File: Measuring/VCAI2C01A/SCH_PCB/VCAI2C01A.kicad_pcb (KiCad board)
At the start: 2 copper layers, 60.5 x 40.1 mm, 74 parts, among them J10 JUMP2_2x1, J11 JUMP2_2x1, J13 JUMP_5X2, J14 JUMP_2x1, J15 JUMP_2x1, J16 JUMP_2x1, J17 JUMP_2x1, J18 JUMP_2x1, J19 JUMP_2x1, J2 CONN_2, J20 JUMP_2x1, J21 JUMP_2x1, J22 JUMP_2x1, J23 JUMP_2x1, J3 JUMP_2x1, J4 CONN_2, J5 JUMP_2x1, J6 CONN_2, J7 JUMP_2x1, J8 CONN_2, J9 JUMP_2x1, M1 HOLE, M2 HOLE, M3 HOLE, M4 HOLE, U1 TLC27L2ID, U2 TLC27L2ID, U3 MCP3424

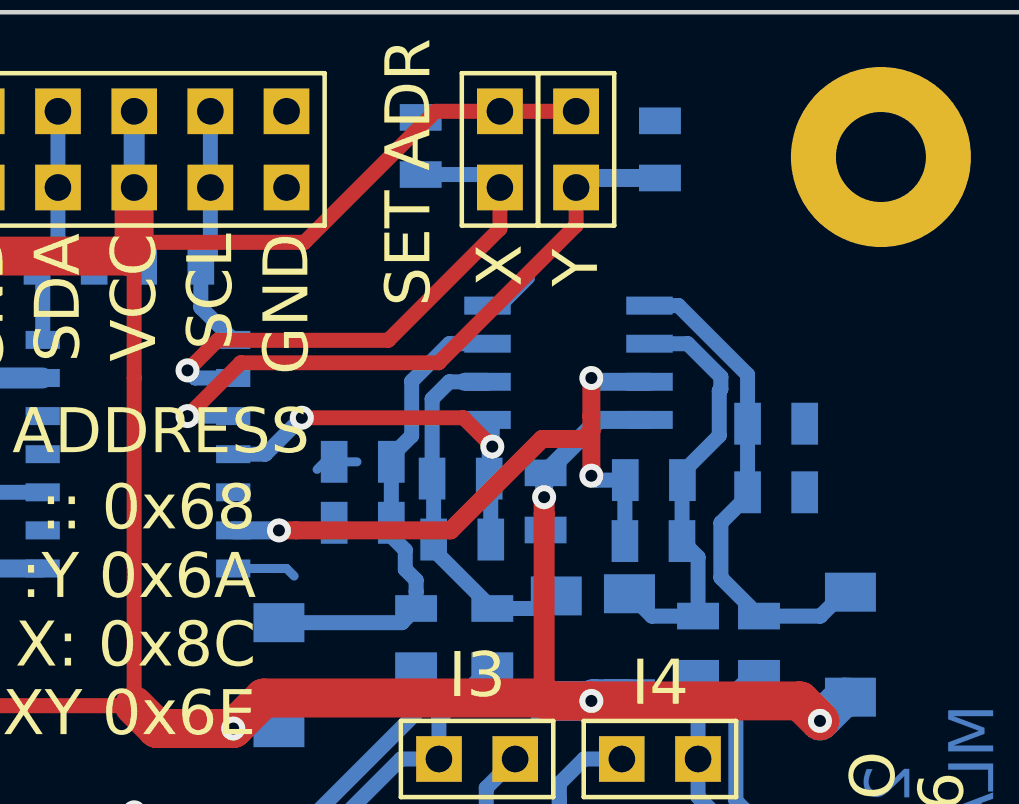
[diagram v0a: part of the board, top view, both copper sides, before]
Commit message: 
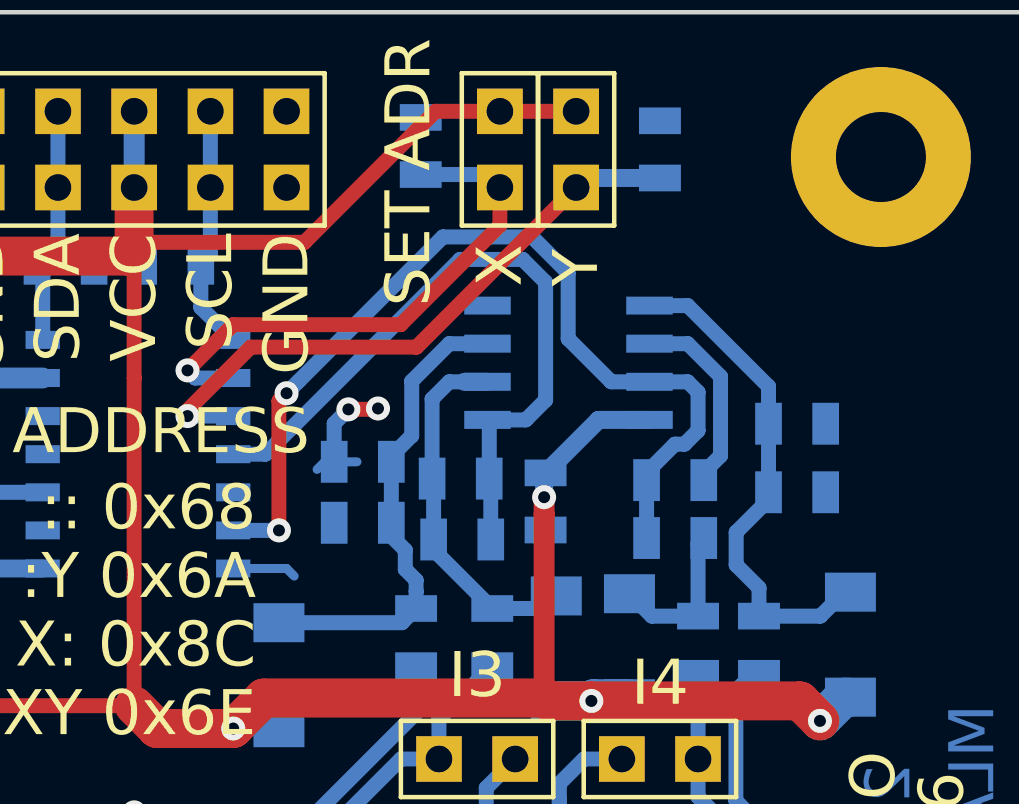
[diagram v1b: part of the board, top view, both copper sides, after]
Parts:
- moved R20 0.73 mm to (49.0, -22.9)
- moved C11 0.71 mm to (49.0, -24.8)
- moved C9 0.70 mm to (53.1, -24.4)
- moved R18 0.70 mm to (53.1, -26.7)
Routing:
- net /OUT3: track 14.0 -> 23.9 mm, vias 2 -> 0
- net /OUT4: track 21.8 -> 31.3 mm, vias 3 -> 2
- net /IN4_2-: track 14.3 -> 11.9 mm
- net GND: track 39.0 -> 40.7 mm, vias 18 -> 20
- net /A1: track 21.3 -> 20.7 mm

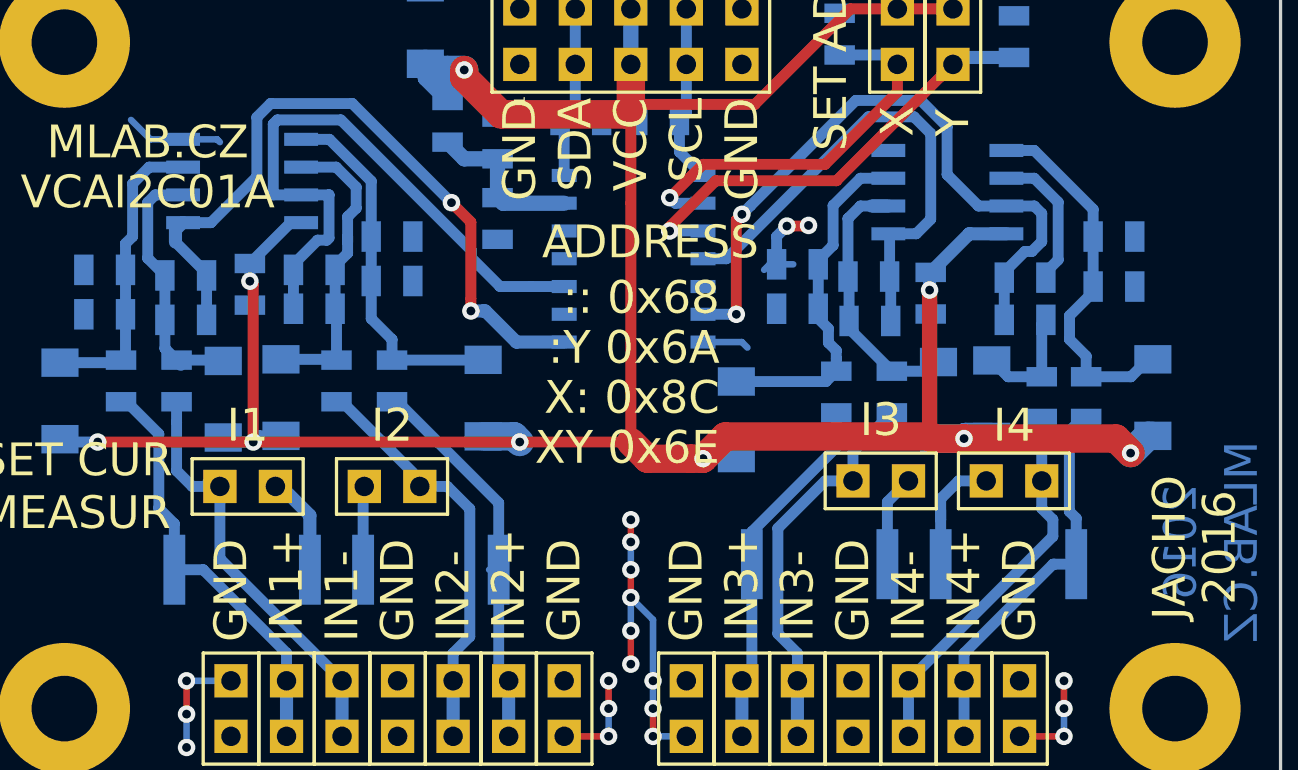
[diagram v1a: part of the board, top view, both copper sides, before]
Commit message: zlepseni layoutu.
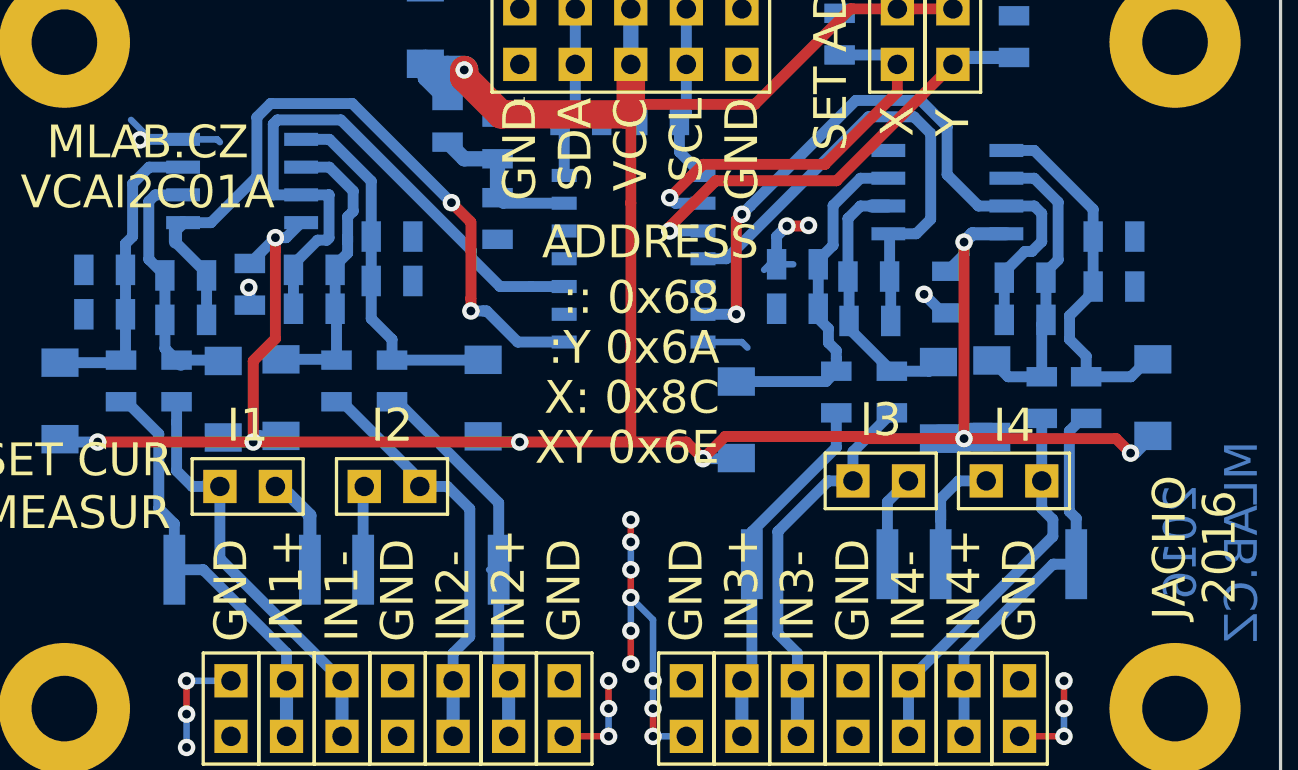
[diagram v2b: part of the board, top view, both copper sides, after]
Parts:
- moved C12 0.76 mm to (45.5, -24.1)
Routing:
- net GND: track 40.7 -> 44.9 mm, vias 20 -> 23
- net VCC: track 141.8 -> 144.9 mm
- net /IN4_2-: track 11.9 -> 13.8 mm

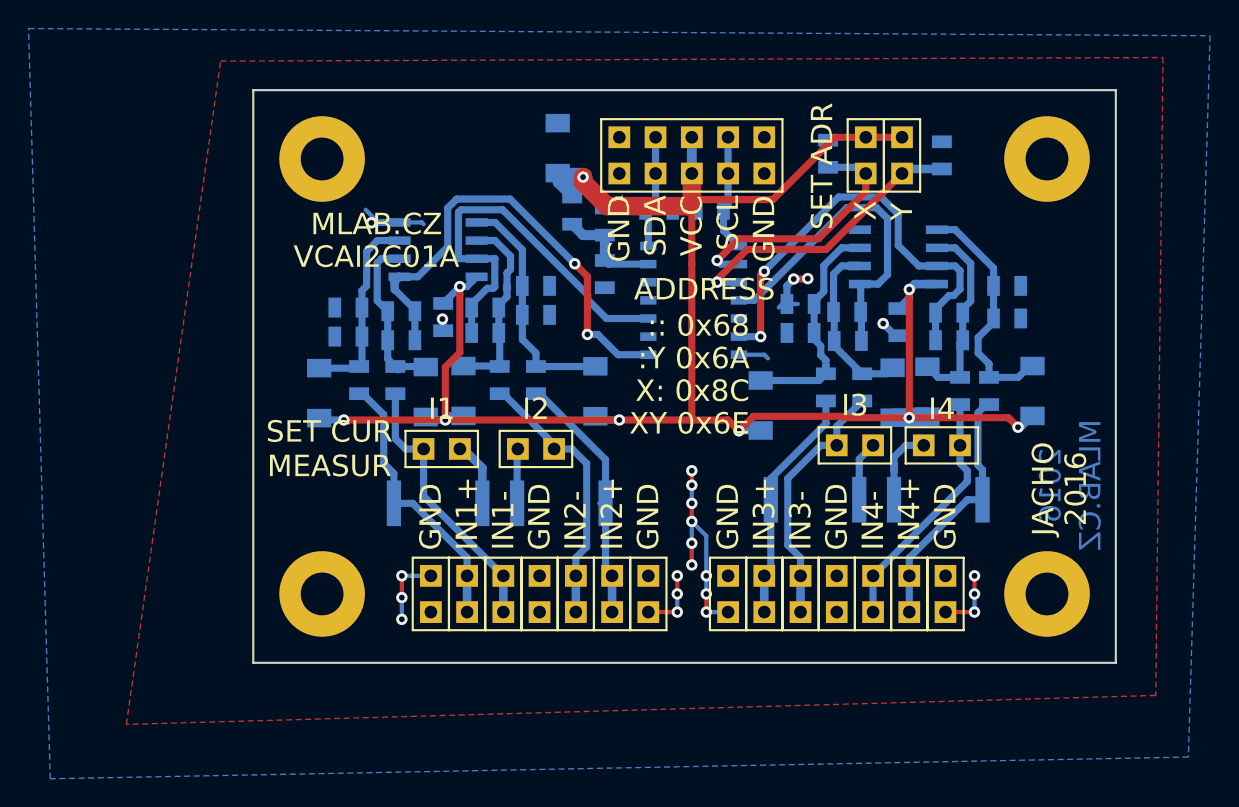
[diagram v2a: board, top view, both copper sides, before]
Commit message: 
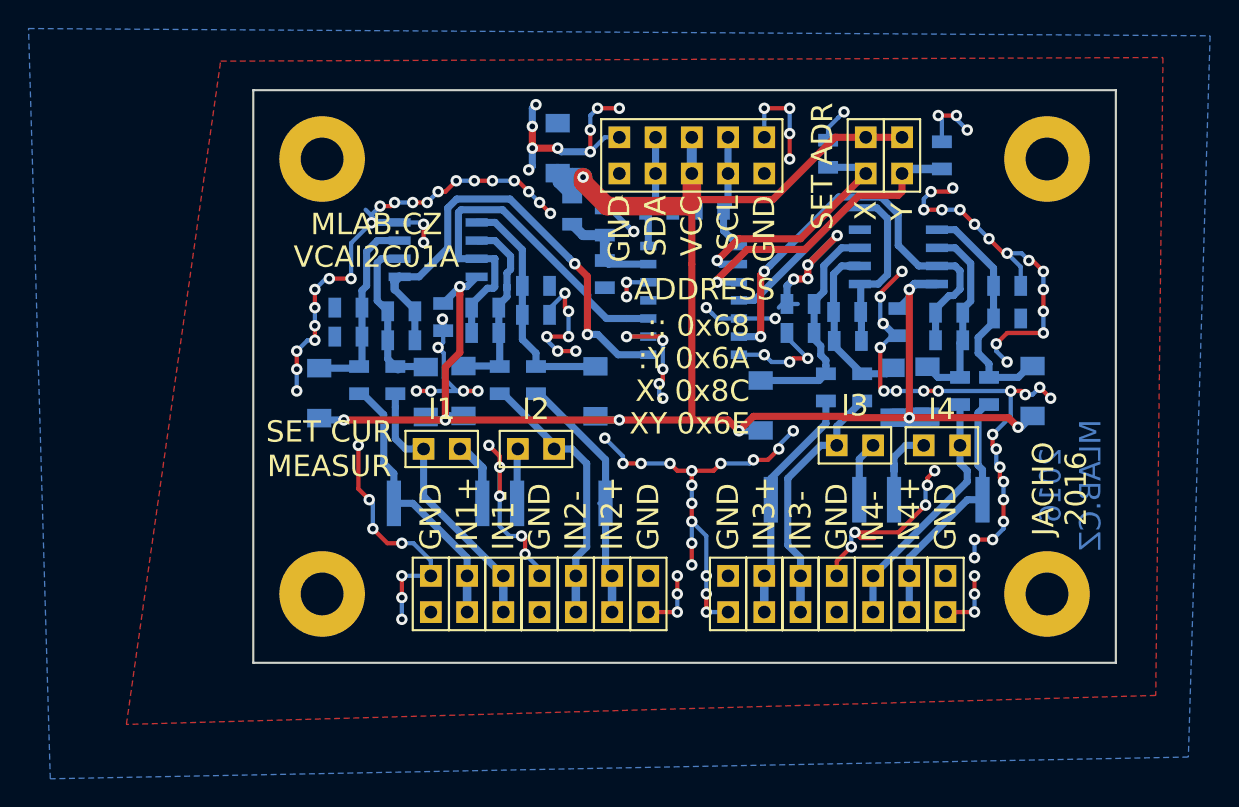
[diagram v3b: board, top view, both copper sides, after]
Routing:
- net GND: track 44.9 -> 277.0 mm, vias 23 -> 146
- net /A1: track 20.7 -> 21.4 mm
- net /A0: track 18.1 -> 17.4 mm

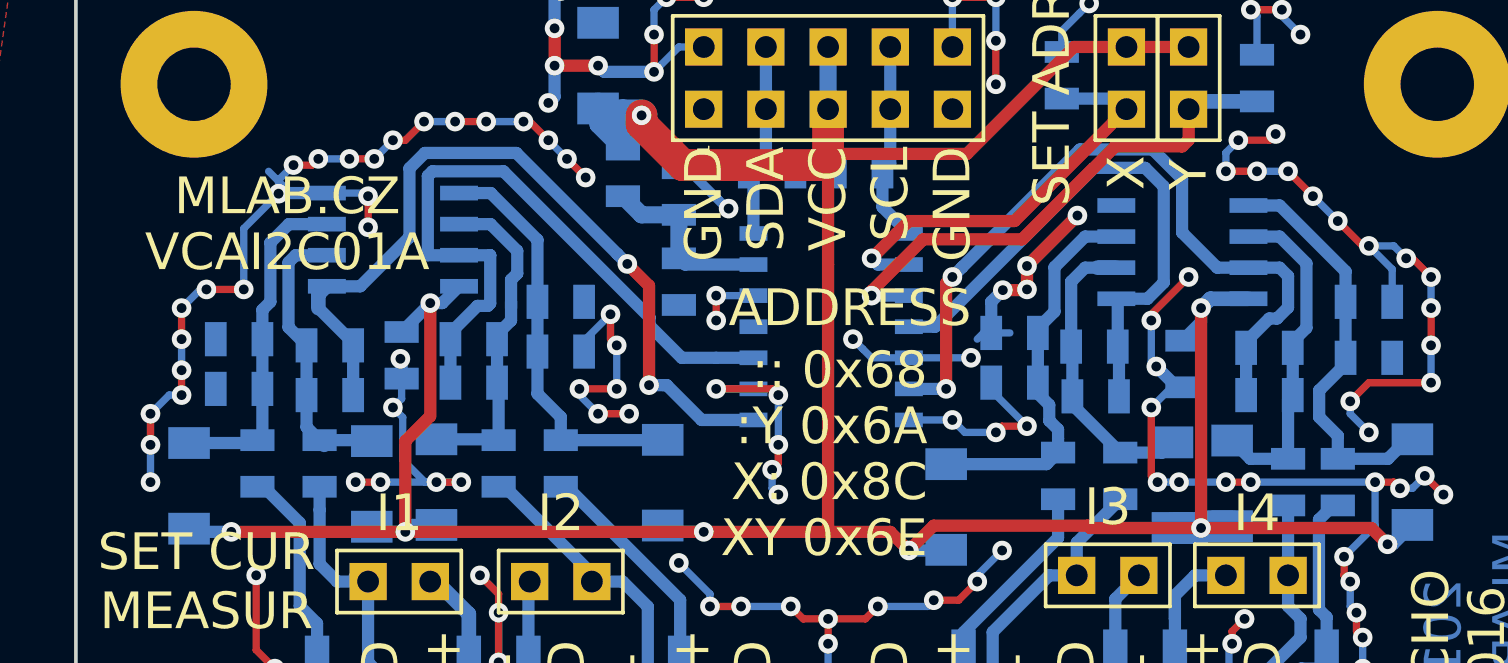
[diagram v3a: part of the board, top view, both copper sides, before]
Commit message: 
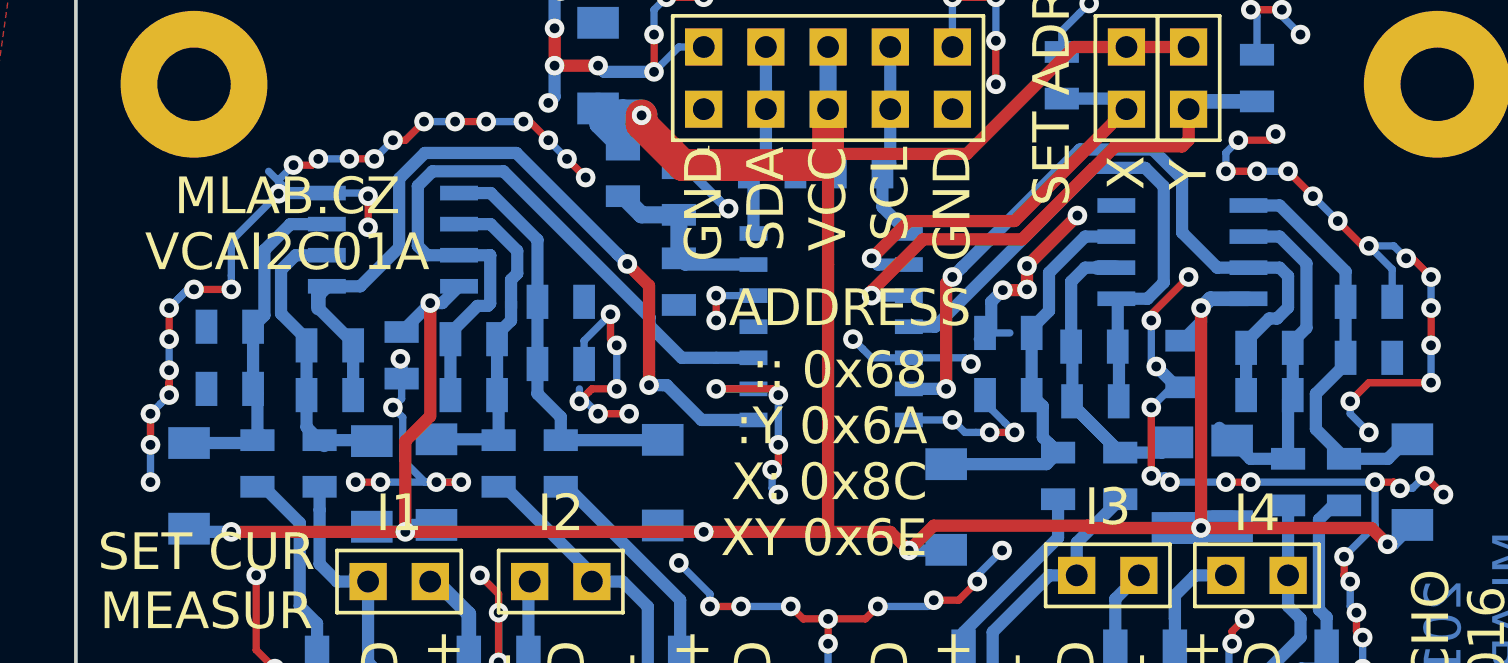
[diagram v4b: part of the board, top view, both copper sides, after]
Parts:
- moved C1 0.63 mm to (6.54, -25.7)
- moved C8 0.57 mm to (38.4, -22.9)
- moved R8 0.51 mm to (20.1, -24.1)
- moved C7 0.51 mm to (16.5, -22.9)
- moved R7 0.38 mm to (6.54, -23.1)
- moved R16 0.25 mm to (52.1, -19.3)
- moved R17 0.25 mm to (38.4, -25.4)
- moved C10 0.20 mm to (41.9, -22.6)
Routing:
- net /IN3_2-: track 13.2 -> 16.1 mm
- net GND: track 277.0 -> 278.8 mm
- net /IN3_2+: track 16.9 -> 17.7 mm
- net /IN4_2-: track 13.8 -> 14.5 mm

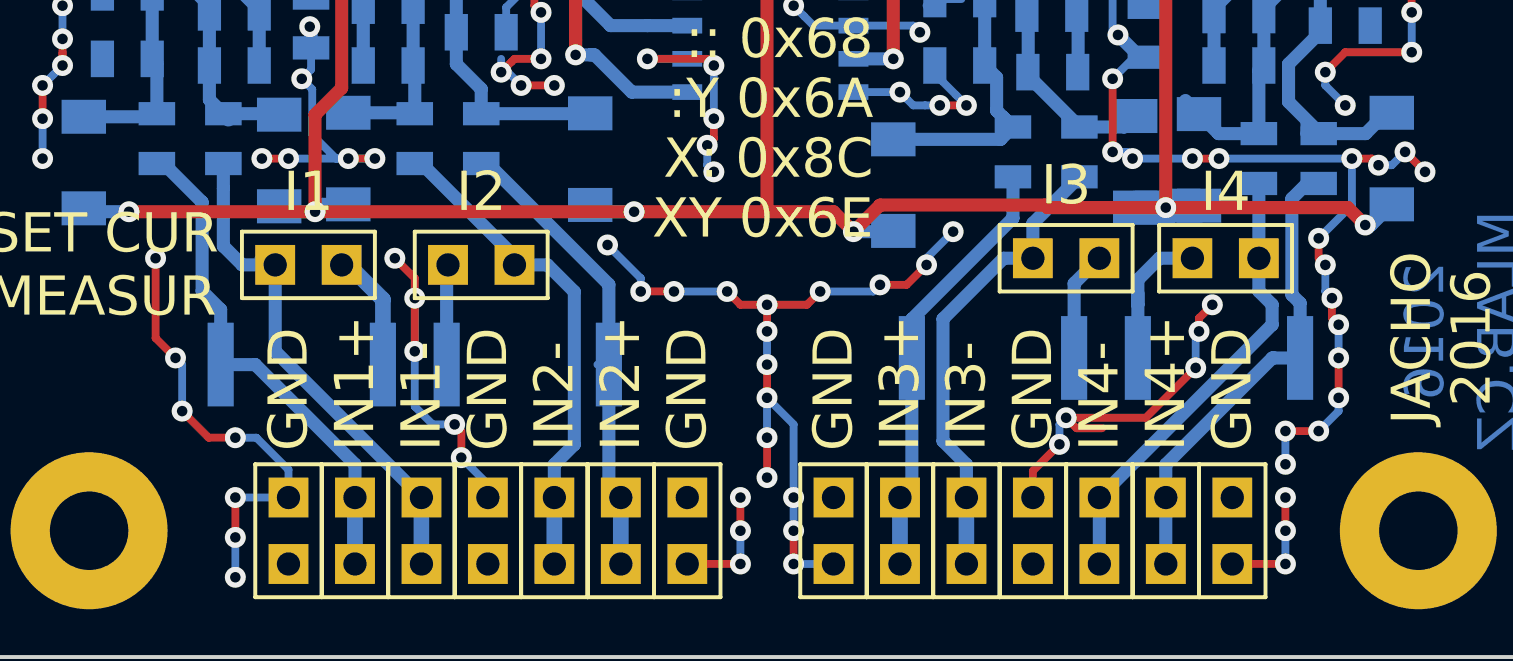
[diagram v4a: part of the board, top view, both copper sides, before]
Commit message: 
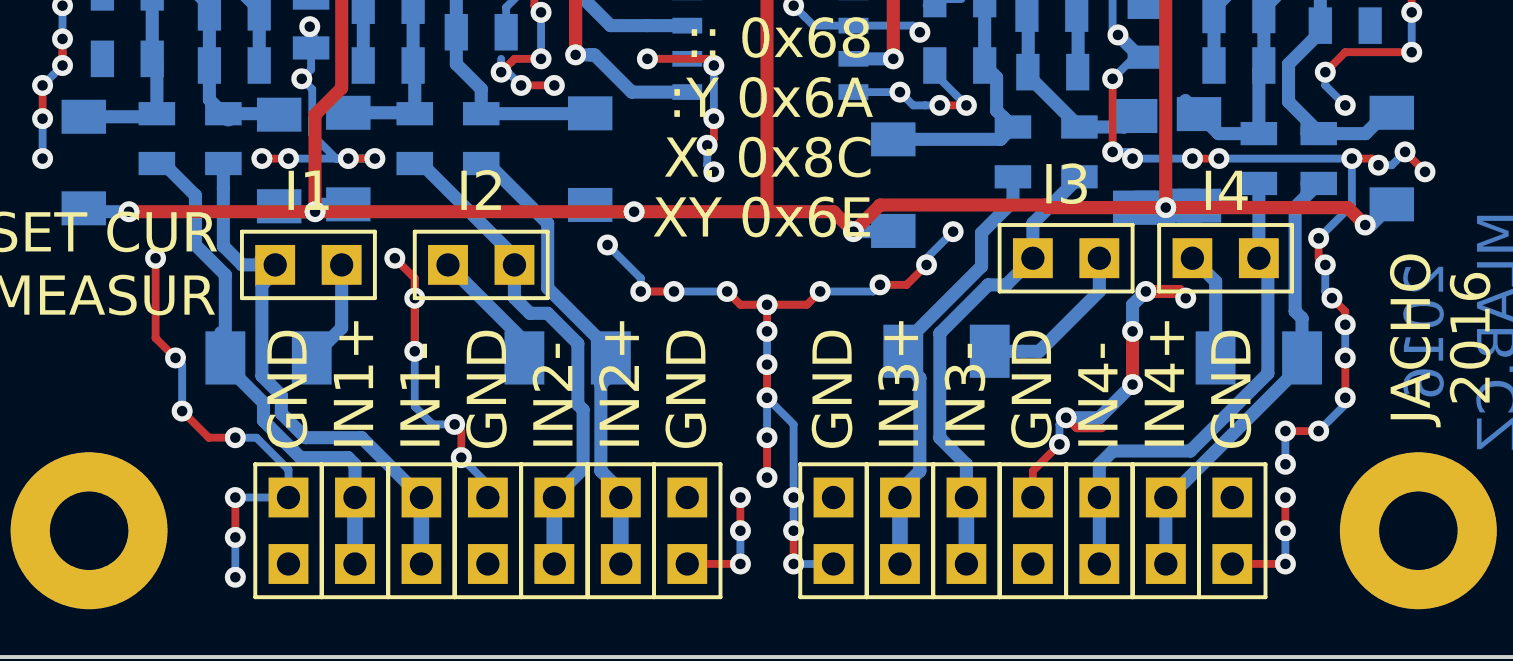
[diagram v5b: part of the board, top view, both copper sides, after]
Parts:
- R1, R11, R12, R2: footprint Mlab_R:SMD-2512 -> Mlab_R:SMD-1206
- moved R11 1.80 mm to (37.8, -11.9)
- moved R2 1.55 mm to (23.4, -11.7)
- moved R12 1.52 mm to (49.8, -11.7)
- moved R1 1.30 mm to (11.9, -11.7)
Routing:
- net Net-(J6-Pad2): track 4.21 -> 6.40 mm
- net Net-(J8-Pad2): track 5.87 -> 4.18 mm
- net /IN1-: track 20.2 -> 21.9 mm
- net /IN4-: track 17.9 -> 19.5 mm
- net /IN3+: track 16.8 -> 18.0 mm
- net Net-(J4-Pad2): track 3.83 -> 4.84 mm
- net /IN2+: track 18.1 -> 19.1 mm
- net Net-(J2-Pad2): track 4.72 -> 4.03 mm
- net GND: track 278.8 -> 279.0 mm, vias 146 -> 147
